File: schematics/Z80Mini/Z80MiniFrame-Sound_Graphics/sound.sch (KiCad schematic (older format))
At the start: 20 parts, among them J3 Conn_01x03_Male, J4 IO_PORT, U7 AY-3-8910, U8 74LS02, U9 LM386, X1 ACO-2MHz

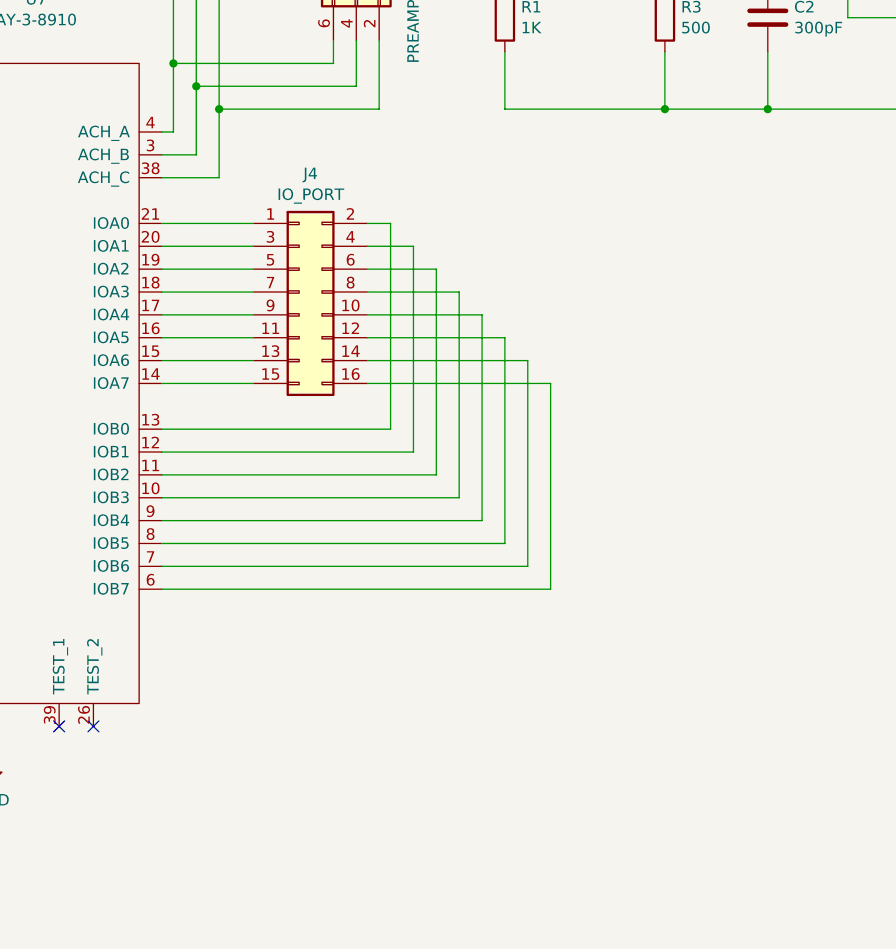
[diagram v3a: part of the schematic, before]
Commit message: Latest modifications and update to v1.1 and first successifully VDP routines test.
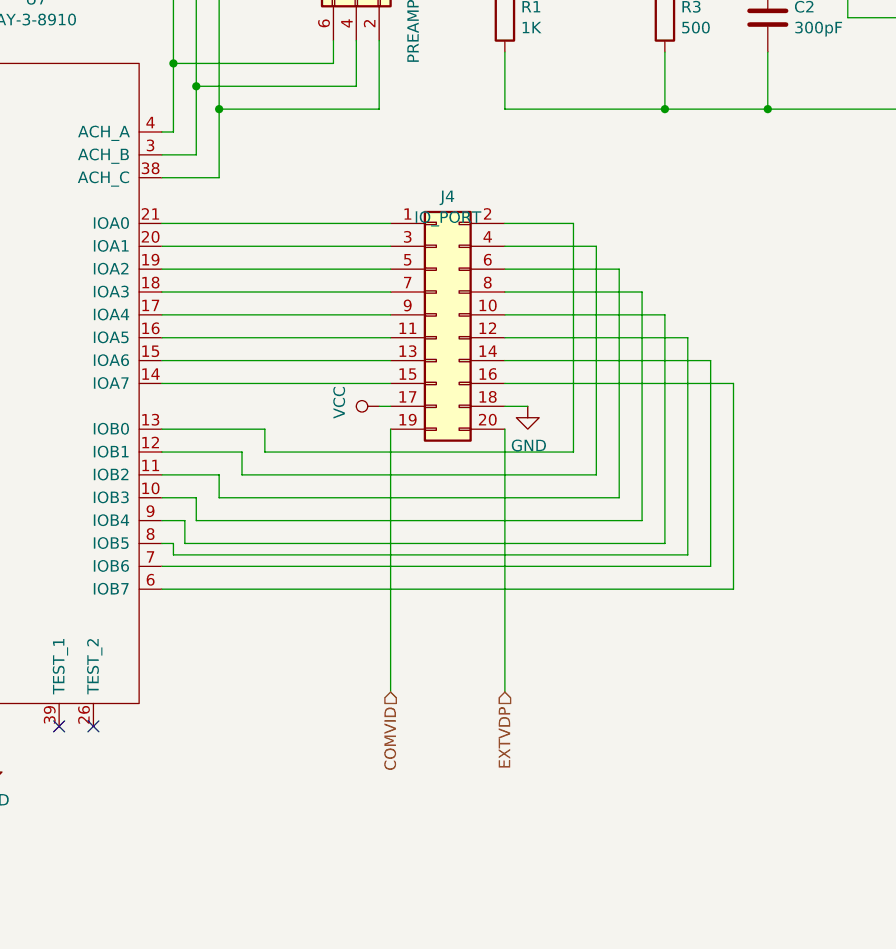
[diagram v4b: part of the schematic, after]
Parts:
- removed J4: IO_PORT, Connector_IDC:IDC-Header_2x08_P2.54mm_Vertical, symbol Connector_Generic:Conn_02x08_Odd_Even
- added J4: IO_PORT, Connector_IDC:IDC-Header_2x10_P2.54mm_Vertical, symbol Connector_Generic:Conn_02x10_Odd_Even
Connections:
- net GND: now also J4.18 (Pin_18)
- net VCC: now also J4.17 (Pin_17)
- net at U7.10 (IOB3): now also J4.8 (Pin_8)
- net at U7.11 (IOB2): now also J4.6 (Pin_6)
- net at U7.12 (IOB1): now also J4.4 (Pin_4)
- net at U7.13 (IOB0): now also J4.2 (Pin_2)
- net at U7.14 (IOA7): now also J4.15 (Pin_15)
- net at U7.15 (IOA6): now also J4.13 (Pin_13)
- net at U7.16 (IOA5): now also J4.11 (Pin_11)
- net at U7.17 (IOA4): now also J4.9 (Pin_9)
- net at U7.18 (IOA3): now also J4.7 (Pin_7)
- net at U7.19 (IOA2): now also J4.5 (Pin_5)
- net at U7.20 (IOA1): now also J4.3 (Pin_3)
- net at U7.21 (IOA0): now also J4.1 (Pin_1)
- net at U7.6 (IOB7): now also J4.16 (Pin_16)
- net at U7.7 (IOB6): now also J4.14 (Pin_14)
- net at U7.8 (IOB5): now also J4.12 (Pin_12)
- net at U7.9 (IOB4): now also J4.10 (Pin_10)
- new net COMVID: J4.19 (Pin_19)
- new net EXTVDP: J4.20 (Pin_20)
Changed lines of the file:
@@
 $Descr A4 11693 8268
 encoding utf-8
-Sheet 4 4
+Sheet 3 3
 Title ""
 Date ""
@@
 $EndComp
 Wire Wire Line
-	5200 3950 5600 3950
-Wire Wire Line
-	5200 4050 5600 4050
-Wire Wire Line
-	5600 4150 5200 4150
-Wire Wire Line
-	5200 4250 5600 4250
-Wire Wire Line
-	5200 4350 5600 4350
-Wire Wire Line
-	5200 4450 5600 4450
-Wire Wire Line
-	5600 4550 5200 4550
-Wire Wire Line
-	5200 4650 5600 4650
-Wire Wire Line
-	5200 4850 6200 4850
-Wire Wire Line
-	6200 4850 6200 3950
-Wire Wire Line
-	6200 3950 6100 3950
-Wire Wire Line
-	6300 4050 6100 4050
-Wire Wire Line
-	5200 4950 6300 4950
-Wire Wire Line
-	6300 4050 6300 4950
-Wire Wire Line
-	5200 5050 6400 5050
-Wire Wire Line
-	6400 5050 6400 4150
-Wire Wire Line
-	6400 4150 6100 4150
-Wire Wire Line
-	5200 5150 6500 5150
-Wire Wire Line
-	6500 5150 6500 4250
-Wire Wire Line
-	6500 4250 6100 4250
-Wire Wire Line
-	5200 5250 6600 5250
-Wire Wire Line
-	6600 5250 6600 4350
-Wire Wire Line
-	6600 4350 6100 4350
-Wire Wire Line
-	5200 5350 6700 5350
-Wire Wire Line
-	6700 5350 6700 4450
-Wire Wire Line
-	6700 4450 6100 4450
-Wire Wire Line
-	5200 5450 6800 5450
-Wire Wire Line
-	6800 5450 6800 4550
-Wire Wire Line
-	6800 4550 6100 4550
-$Comp
-L Connector_Generic:Conn_02x08_Odd_Even J4
-U 1 1 5D817986
-P 5800 4250
-F 0 "J4" H 5850 4767 50  0000 C CNN
-F 1 "IO_PORT" H 5850 4676 50  0000 C CNN
-F 2 "Connector_IDC:IDC-Header_2x08_P2.54mm_Vertical" H 5800 4250 50  0001 C CNN
-F 3 "~" H 5800 4250 50  0001 C CNN
-	1    5800 4250
-	1    0    0    -1
-$EndComp
-Wire Wire Line
-	5200 5550 6900 5550
-Wire Wire Line
-	6900 5550 6900 4650
-Wire Wire Line
-	6100 4650 6900 4650
+	7600 5450 7600 4550
+$Comp
+L Connector_Generic:Conn_02x10_Odd_Even J4
+U 1 1 5E15F856
+P 6400 4350
+AR Path="/5D76ACBB/5E15F856" Ref="J4"  Part="1"
+AR Path="/5E15F856" Ref="J?"  Part="1"
+F 0 "J4" H 6450 4867 50  0000 C CNN
+F 1 "IO_PORT" H 6450 4776 50  0000 C CNN
+F 2 "Connector_IDC:IDC-Header_2x10_P2.54mm_Vertical" H 6400 4350 50  0001 C CNN
+F 3 "~" H 6400 4350 50  0001 C CNN
+	1    6400 4350
+	1    0    0    -1
+$EndComp
+Wire Wire Line
+	7700 5550 7700 4650
+$Comp
+L power:GND #PWR0130
+U 1 1 5E15F85F
+P 6800 4750
+AR Path="/5D76ACBB/5E15F85F" Ref="#PWR0130"  Part="1"
+AR Path="/5E15F85F" Ref="#PWR?"  Part="1"
+F 0 "#PWR0130" H 6800 4500 50  0001 C CNN
+F 1 "GND" H 6805 4577 50  0000 C CNN
+F 2 "" H 6800 4750 50  0001 C CNN
+F 3 "" H 6800 4750 50  0001 C CNN
+	1    6800 4750
+	1    0    0    -1
+$EndComp
+Wire Wire Line
+	6700 4750 6800 4750
+$Comp
+L power:VCC #PWR?
+U 1 1 5E15F866
+P 6150 4750
+AR Path="/5E15F866" Ref="#PWR?"  Part="1"
+AR Path="/5D76ACBB/5E15F866" Ref="#PWR0131"  Part="1"
+F 0 "#PWR0131" H 6150 4600 50  0001 C CNN
+F 1 "VCC" H 6167 4923 50  0000 C CNN
+F 2 "" H 6150 4750 50  0001 C CNN
+F 3 "" H 6150 4750 50  0001 C CNN
+	1    6150 4750
+	0    -1   -1   0
+$EndComp
+Wire Wire Line
+	5200 3950 6200 3950
+Wire Wire Line
+	5200 4050 6200 4050
+Wire Wire Line
+	5200 4150 6200 4150
+Wire Wire Line
+	5200 4250 6200 4250
+Wire Wire Line
+	5200 4350 6200 4350
+Wire Wire Line
+	5200 4450 6200 4450
+Wire Wire Line
+	5200 4550 6200 4550
+Wire Wire Line
+	5200 4650 6200 4650
+Wire Wire Line
+	6150 4750 6200 4750
+Wire Wire Line
+	6200 4850 6200 6000
+Wire Wire Line
+	6700 4850 6700 6000
+Text HLabel 6200 6000 3    50   Input ~ 0
+COMVID
+Text HLabel 6700 6000 3    50   Input ~ 0
+EXTVDP
+Wire Wire Line
+	6700 4050 7100 4050
+Wire Wire Line
+	6700 4150 7200 4150
+Wire Wire Line
+	6700 4250 7300 4250
+Wire Wire Line
+	6700 4350 7400 4350
+Wire Wire Line
+	6700 4450 7500 4450
+Wire Wire Line
+	6700 4550 7600 4550
+Wire Wire Line
+	6700 4650 7700 4650
+Wire Wire Line
+	6700 3950 7000 3950
+Wire Wire Line
+	7000 3950 7000 4950
+Wire Wire Line
+	7000 4950 5650 4950
+Wire Wire Line
+	5650 4950 5650 4850
+Wire Wire Line
+	5650 4850 5200 4850
+Wire Wire Line
+	7100 5050 5550 5050
+Wire Wire Line
+	5550 5050 5550 4950
+Wire Wire Line
+	5550 4950 5200 4950
+Wire Wire Line
+	7100 4050 7100 5050
+Wire Wire Line
+	5200 5050 5450 5050
+Wire Wire Line
+	5450 5050 5450 5150
+Wire Wire Line
+	5450 5150 7200 5150
+Wire Wire Line
+	7200 4150 7200 5150
+Wire Wire Line
+	7300 5250 5350 5250
+Wire Wire Line
+	5350 5250 5350 5150
+Wire Wire Line
+	5350 5150 5200 5150
+Wire Wire Line
+	7300 4250 7300 5250
+Wire Wire Line
+	5200 5250 5300 5250
+Wire Wire Line
+	5300 5250 5300 5350
+Wire Wire Line
+	5300 5350 7400 5350
+Wire Wire Line
+	7400 4350 7400 5350
+Wire Wire Line
+	7500 5400 5250 5400
+Wire Wire Line
+	5250 5400 5250 5350
+Wire Wire Line
+	5250 5350 5200 5350
+Wire Wire Line
+	7500 4450 7500 5400
+Wire Wire Line
+	5200 5450 7600 5450
+Wire Wire Line
+	5200 5550 7700 5550
 Wire Bus Line
 	3900 3000 3900 4150

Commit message: Testing C routines for VDP and keyboard. Generated backplane gerber files
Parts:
- added JP4: Jumper_NC_Dual, Connector_PinHeader_2.54mm:PinHeader_1x03_P2.54mm_Vertical, symbol Device:Jumper_NC_Dual
- J3: footprint Connector_PinHeader_2.00mm:PinHeader_1x03_P2.00mm_Vertical -> Connector_PinHeader_2.54mm:PinHeader_1x03_P2.54mm_Vertical
- JP1: footprint Connector_PinHeader_2.00mm:PinHeader_2x03_P2.00mm_Vertical -> Connector_PinHeader_2.54mm:PinHeader_2x03_P2.54mm_Vertical
- SPEAKER1: footprint Connector_Wire:SolderWirePad_1x02_P3.81mm_Drill1mm -> Connector_PinHeader_2.54mm:PinHeader_1x02_P2.54mm_Vertical
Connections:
- net labels added: CPUCLK
- wire segments 145 -> 146
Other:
- moved on the sheet: X1
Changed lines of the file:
@@
 F 0 "SPEAKER1" H 10472 2732 50  0000 R CNN
 F 1 "Conn_01x02_Male" H 10472 2823 50  0000 R CNN
-F 2 "Connector_Wire:SolderWirePad_1x02_P3.81mm_Drill1mm" H 10500 2850 50  0001 C CNN
+F 2 "Connector_PinHeader_2.54mm:PinHeader_1x02_P2.54mm_Vertical" H 10500 2850 50  0001 C CNN
 F 3 "~" H 10500 2850 50  0001 C CNN
 	1    10500 2850
@@
 L Oscillator:ACO-xxxMHz X1
 U 1 1 5E3763A5
-P 3550 6800
-F 0 "X1" H 3207 6846 50  0000 R CNN
-F 1 "ACO-2MHz" H 3207 6755 50  0000 R CNN
-F 2 "Oscillator:Oscillator_DIP-14" H 4000 6450 50  0001 C CNN
-F 3 "http://www.conwin.com/datasheets/cx/cx030.pdf" H 3450 6800 50  0001 C CNN
-	1    3550 6800
-	1    0    0    -1
-$EndComp
-Wire Wire Line
-	3900 6800 3850 6800
+P 3250 6900
+F 0 "X1" H 2907 6946 50  0000 R CNN
+F 1 "ACO-2MHz" H 2907 6855 50  0000 R CNN
+F 2 "Oscillator:Oscillator_DIP-14" H 3700 6550 50  0001 C CNN
+F 3 "http://www.conwin.com/datasheets/cx/cx030.pdf" H 3150 6900 50  0001 C CNN
+	1    3250 6900
+	1    0    0    -1
+$EndComp
 Wire Wire Line
 	3900 5150 3900 6800
@@
 L power:VCC #PWR0147
 U 1 1 5E37FE16
-P 3550 6400
-F 0 "#PWR0147" H 3550 6250 50  0001 C CNN
-F 1 "VCC" H 3567 6573 50  0000 C CNN
-F 2 "" H 3550 6400 50  0001 C CNN
-F 3 "" H 3550 6400 50  0001 C CNN
-	1    3550 6400
+P 3250 6500
+F 0 "#PWR0147" H 3250 6350 50  0001 C CNN
+F 1 "VCC" H 3267 6673 50  0000 C CNN
+F 2 "" H 3250 6500 50  0001 C CNN
+F 3 "" H 3250 6500 50  0001 C CNN
+	1    3250 6500
 	1    0    0    -1
 $EndComp
@@
 L power:GND #PWR0148
 U 1 1 5E380313
-P 3550 7200
-F 0 "#PWR0148" H 3550 6950 50  0001 C CNN
-F 1 "GND" H 3555 7027 50  0000 C CNN
-F 2 "" H 3550 7200 50  0001 C CNN
-F 3 "" H 3550 7200 50  0001 C CNN
-	1    3550 7200
-	1    0    0    -1
-$EndComp
-Wire Wire Line
-	3550 6500 3550 6400
-Wire Wire Line
-	3550 7200 3550 7100
+P 3250 7300
+F 0 "#PWR0148" H 3250 7050 50  0001 C CNN
+F 1 "GND" H 3255 7127 50  0000 C CNN
+F 2 "" H 3250 7300 50  0001 C CNN
+F 3 "" H 3250 7300 50  0001 C CNN
+	1    3250 7300
+	1    0    0    -1
+$EndComp
+Wire Wire Line
+	3250 6600 3250 6500
+Wire Wire Line
+	3250 7300 3250 7200
 Wire Wire Line
 	7850 3450 8700 3450
@@
 F 0 "JP1" V 6100 2650 50  0000 R CNN
 F 1 "PREAMP_MONO" H 6450 3100 50  0000 R CNN
-F 2 "Connector_PinHeader_2.00mm:PinHeader_2x03_P2.00mm_Vertical" H 6050 2850 50  0001 C CNN
+F 2 "Connector_PinHeader_2.54mm:PinHeader_2x03_P2.54mm_Vertical" H 6050 2850 50  0001 C CNN
 F 3 "~" H 6050 2850 50  0001 C CNN
 	1    6050 2850
@@
 F 0 "J3" V 5412 2544 50  0000 L CNN
 F 1 "Conn_01x03_Male" V 5503 2544 50  0000 L CNN
-F 2 "Connector_PinHeader_2.00mm:PinHeader_1x03_P2.00mm_Vertical" H 5350 2400 50  0001 C CNN
+F 2 "Connector_PinHeader_2.54mm:PinHeader_1x03_P2.54mm_Vertical" H 5350 2400 50  0001 C CNN
 F 3 "~" H 5350 2400 50  0001 C CNN
 	1    5350 2400
@@
 Wire Wire Line
 	5200 5550 7700 5550
+$Comp
+L Device:Jumper_NC_Dual JP?
+U 1 1 5E21D650
+P 3900 6900
+AR Path="/5E21D650" Ref="JP?"  Part="1"
+AR Path="/5D76ACBB/5E21D650" Ref="JP4"  Part="1"
+F 0 "JP4" H 3900 7047 50  0000 C CNN
+F 1 "Jumper_NC_Dual" H 3900 7138 50  0000 C CNN
+F 2 "Connector_PinHeader_2.54mm:PinHeader_1x03_P2.54mm_Vertical" H 3900 6900 50  0001 C CNN
+F 3 "~" H 3900 6900 50  0001 C CNN
+	1    3900 6900
+	-1   0    0    1
+$EndComp
+Wire Wire Line
+	3550 6900 3650 6900
+Wire Wire Line
+	4150 6900 4700 6900
 Wire Bus Line
 	3900 3000 3900 4150
+Text HLabel 4700 6900 2    50   Input ~ 0
+CPUCLK
 $EndSCHEMATC

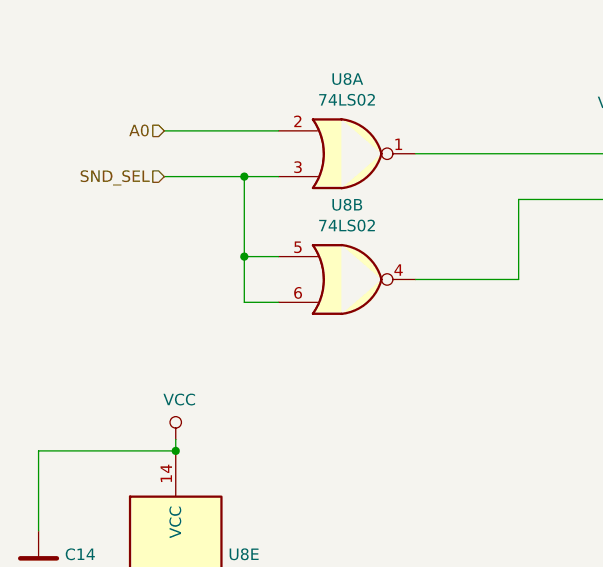
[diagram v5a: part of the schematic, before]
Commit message: Latest code changes and modified Makefile to support burn to EPROM Emulator
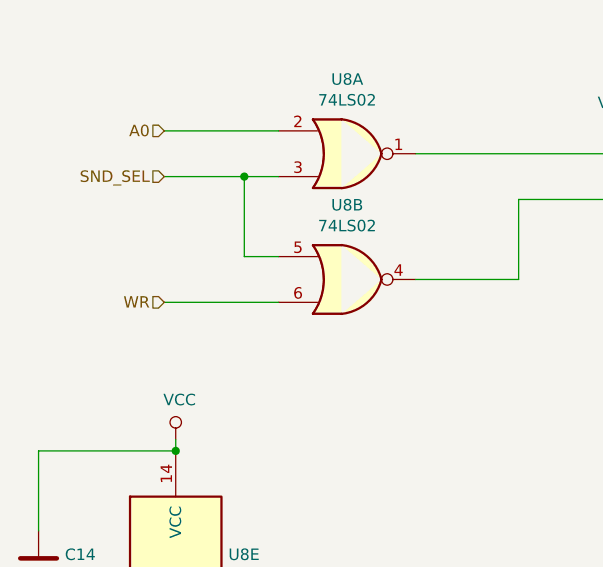
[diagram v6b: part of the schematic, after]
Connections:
- net labels added: WR
- wire segments 146 -> 145
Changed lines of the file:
@@
 EESchema Schematic File Version 4
-LIBS:Z80MiniFrame-Sound_Graphics-cache
 EELAYER 30 0
 EELAYER END
@@
 	3250 5000 2800 5000
 Wire Wire Line
-	2200 5100 2050 5100
-Wire Wire Line
-	2050 5100 2050 4900
-Wire Wire Line
 	2050 4900 2200 4900
 Wire Wire Line
@@
 Wire Wire Line
 	2050 4550 2050 4900
-Connection ~ 2050 4900
 Wire Wire Line
 	2200 4350 1700 4350
@@
 Wire Wire Line
 	4150 6900 4700 6900
+Text HLabel 4700 6900 2    50   Input ~ 0
+CPUCLK
+Wire Wire Line
+	1700 5100 2200 5100
 Wire Bus Line
 	3900 3000 3900 4150
-Text HLabel 4700 6900 2    50   Input ~ 0
-CPUCLK
+Text HLabel 1700 5100 0    50   Input ~ 0
+WR
 $EndSCHEMATC
